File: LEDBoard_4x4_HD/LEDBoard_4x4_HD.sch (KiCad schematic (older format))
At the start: 24 parts, among them J1 power, J2 data, U1 TLC5957

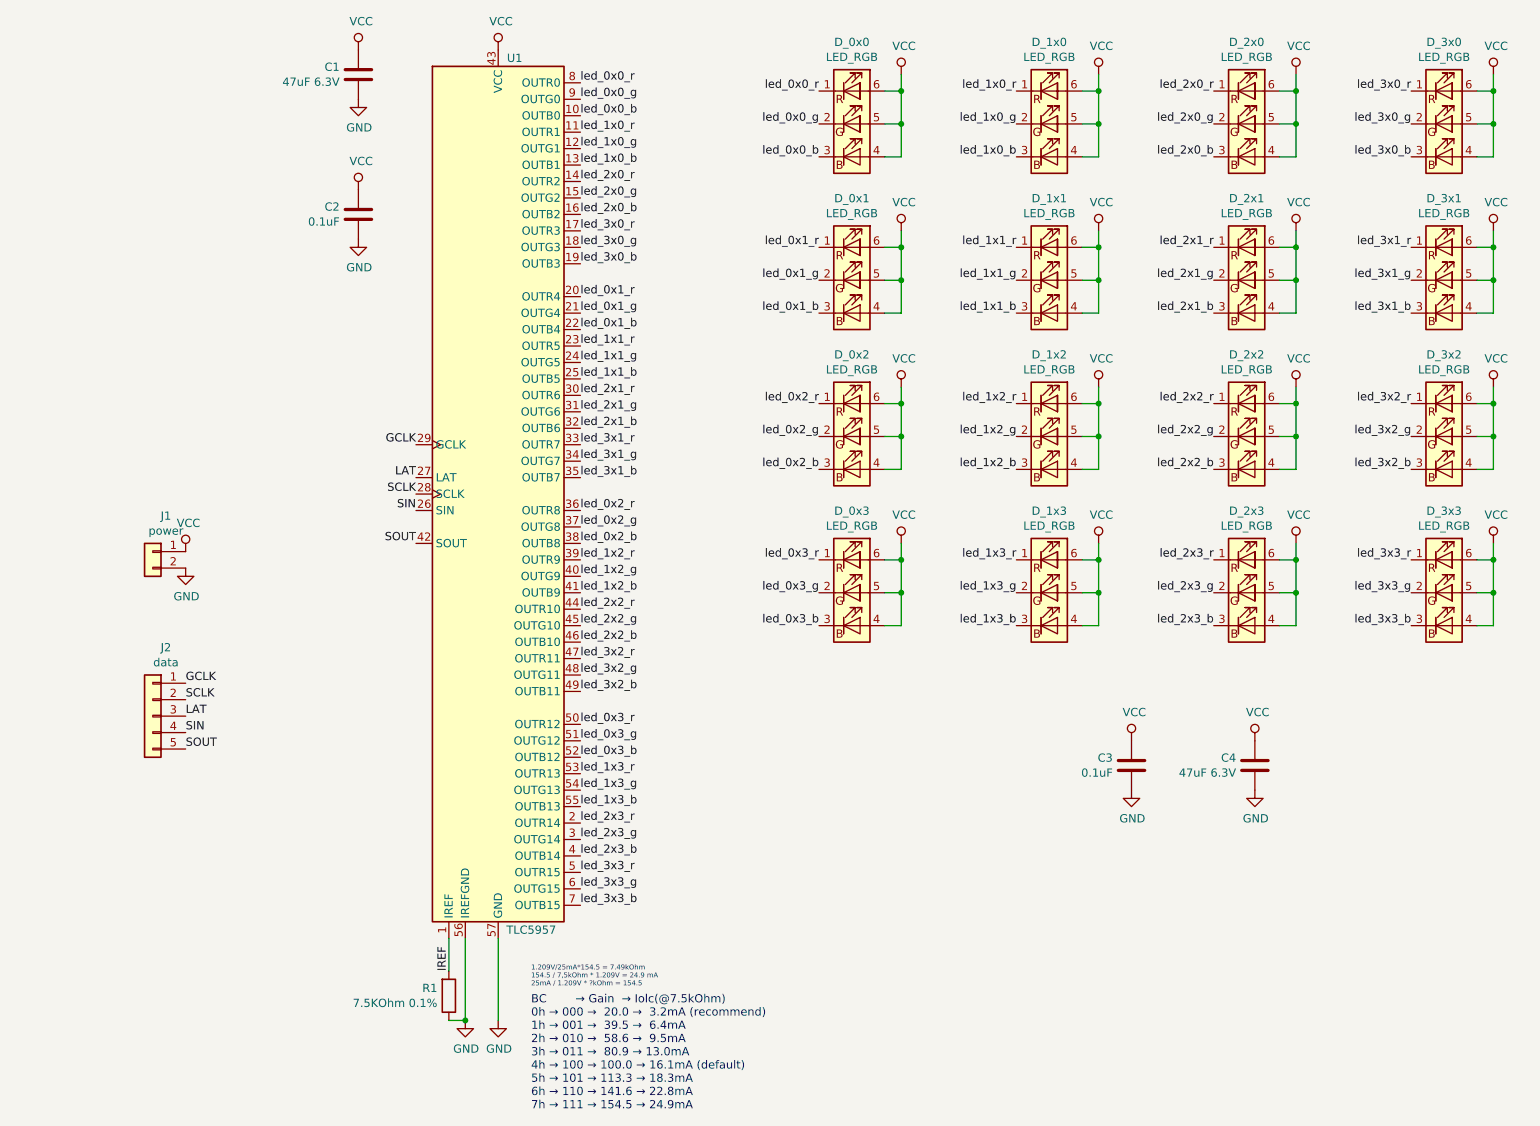
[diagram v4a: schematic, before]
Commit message: more layout tweeks + separate VCC for controler
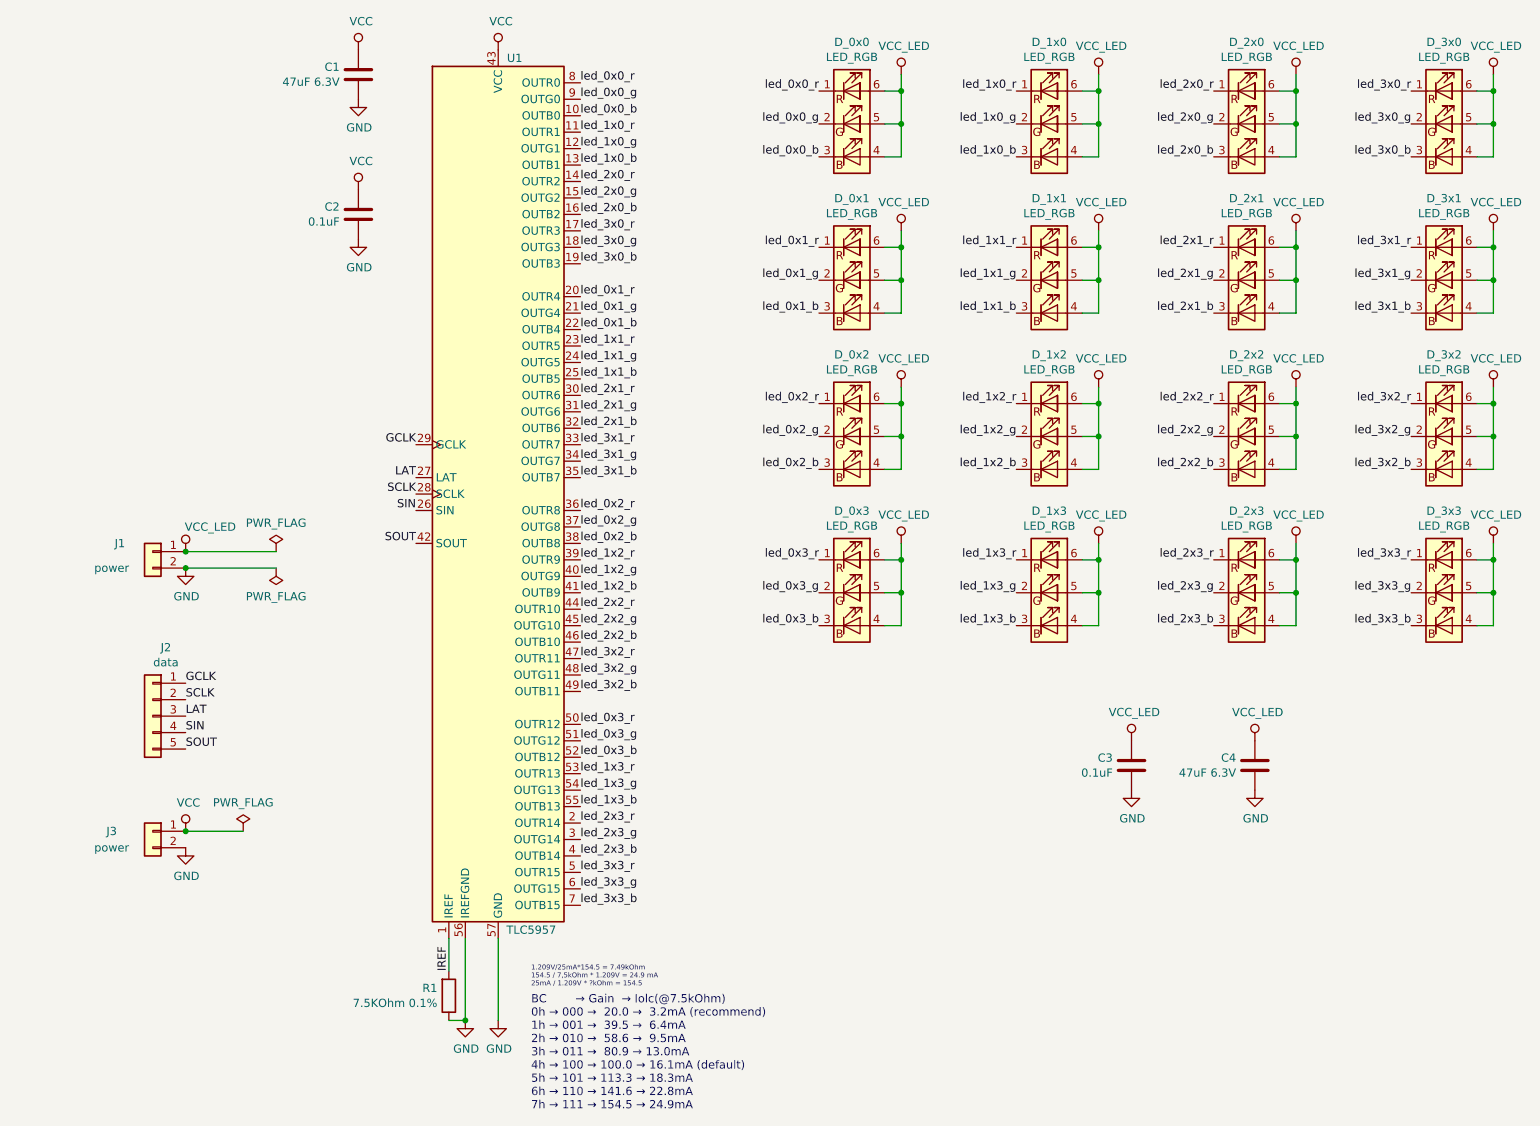
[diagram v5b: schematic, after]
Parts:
- added J3: power, PCB_SolderMount:Conn_01x02_SMD_90deg_SolderMount, symbol Connector_Generic:Conn_01x02
- J1: footprint Connector_PinHeader_2.54mm:PinHeader_1x02_P2.54mm_Vertical -> PCB_SolderMount:Conn_01x02_SMD_90deg_SolderMount
- J2: footprint Connector_PinHeader_2.54mm:PinHeader_1x05_P2.54mm_Vertical -> PCB_SolderMount:Conn_01x05_SMD_90deg_SolderMount
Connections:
- net GND: now also J3.2 (Pin_2)
- net VCC: now also J3.1 (Pin_1); no longer C3.2, C4.2, D_0x0.4 (BA), D_0x0.5 (GA), D_0x0.6 (RA), D_0x1.4 (BA), D_0x1.5 (GA), D_0x1.6 (RA), D_0x2.4 (BA), D_0x2.5 (GA), D_0x2.6 (RA), D_0x3.4 (BA), D_0x3.5 (GA), D_0x3.6 (RA), D_1x0.4 (BA), D_1x0.5 (GA), D_1x0.6 (RA), D_1x1.4 (BA), D_1x1.5 (GA), D_1x1.6 (RA), D_1x2.4 (BA), D_1x2.5 (GA), D_1x2.6 (RA), D_1x3.4 (BA), D_1x3.5 (GA), D_1x3.6 (RA), D_2x0.4 (BA), D_2x0.5 (GA), D_2x0.6 (RA), D_2x1.4 (BA), D_2x1.5 (GA), D_2x1.6 (RA), D_2x2.4 (BA), D_2x2.5 (GA), D_2x2.6 (RA), D_2x3.4 (BA), D_2x3.5 (GA), D_2x3.6 (RA), D_3x0.4 (BA), D_3x0.5 (GA), D_3x0.6 (RA), D_3x1.4 (BA), D_3x1.5 (GA), D_3x1.6 (RA), D_3x2.4 (BA), D_3x2.5 (GA), D_3x2.6 (RA), D_3x3.4 (BA), D_3x3.5 (GA), D_3x3.6 (RA), J1.1 (Pin_1)
- new net VCC_LED: C3.2, C4.2, D_0x0.4 (BA), D_0x0.5 (GA), D_0x0.6 (RA), D_0x1.4 (BA), D_0x1.5 (GA), D_0x1.6 (RA), D_0x2.4 (BA), D_0x2.5 (GA), D_0x2.6 (RA), D_0x3.4 (BA), D_0x3.5 (GA), D_0x3.6 (RA), D_1x0.4 (BA), D_1x0.5 (GA), D_1x0.6 (RA), D_1x1.4 (BA), D_1x1.5 (GA), D_1x1.6 (RA), D_1x2.4 (BA), D_1x2.5 (GA), D_1x2.6 (RA), D_1x3.4 (BA), D_1x3.5 (GA), D_1x3.6 (RA), D_2x0.4 (BA), D_2x0.5 (GA), D_2x0.6 (RA), D_2x1.4 (BA), D_2x1.5 (GA), D_2x1.6 (RA), D_2x2.4 (BA), D_2x2.5 (GA), D_2x2.6 (RA), D_2x3.4 (BA), D_2x3.5 (GA), D_2x3.6 (RA), D_3x0.4 (BA), D_3x0.5 (GA), D_3x0.6 (RA), D_3x1.4 (BA), D_3x1.5 (GA), D_3x1.6 (RA), D_3x2.4 (BA), D_3x2.5 (GA), D_3x2.6 (RA), D_3x3.4 (BA), D_3x3.5 (GA), D_3x3.6 (RA), J1.1 (Pin_1)
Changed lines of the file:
@@
 $EndComp
 $Comp
-L power:VCC #PWR0101
+L VCC_LED:VCC_LED #PWR0101
 U 1 1 5BC4D9F4
 P 7250 1900
 F 0 "#PWR0101" H 7250 1750 50  0001 C CNN
-F 1 "VCC" H 7267 2073 50  0000 C CNN
+F 1 "VCC_LED" H 7267 2073 50  0000 C CNN
 F 2 "" H 7250 1900 50  0001 C CNN
 F 3 "" H 7250 1900 50  0001 C CNN
@@
 $EndComp
 $Comp
-L power:VCC #PWR0102
+L VCC_LED:VCC_LED #PWR0102
 U 1 1 5BC4DBAD
 P 7250 950
 F 0 "#PWR0102" H 7250 800 50  0001 C CNN
-F 1 "VCC" H 7267 1123 50  0000 C CNN
+F 1 "VCC_LED" H 7267 1123 50  0000 C CNN
 F 2 "" H 7250 950 50  0001 C CNN
 F 3 "" H 7250 950 50  0001 C CNN
@@
 $EndComp
 $Comp
-L power:VCC #PWR0103
+L VCC_LED:VCC_LED #PWR0103
 U 1 1 5BC4DCEA
 P 7250 3800
 F 0 "#PWR0103" H 7250 3650 50  0001 C CNN
-F 1 "VCC" H 7267 3973 50  0000 C CNN
+F 1 "VCC_LED" H 7267 3973 50  0000 C CNN
 F 2 "" H 7250 3800 50  0001 C CNN
 F 3 "" H 7250 3800 50  0001 C CNN
@@
 $EndComp
 $Comp
-L power:VCC #PWR0104
+L VCC_LED:VCC_LED #PWR0104
 U 1 1 5BC4DD01
 P 7250 2850
 F 0 "#PWR0104" H 7250 2700 50  0001 C CNN
-F 1 "VCC" H 7267 3023 50  0000 C CNN
+F 1 "VCC_LED" H 7267 3023 50  0000 C CNN
 F 2 "" H 7250 2850 50  0001 C CNN
 F 3 "" H 7250 2850 50  0001 C CNN
@@
 $EndComp
 $Comp
-L power:VCC #PWR0105
+L VCC_LED:VCC_LED #PWR0105
 U 1 1 5BC4E1D5
 P 8450 1900
 F 0 "#PWR0105" H 8450 1750 50  0001 C CNN
-F 1 "VCC" H 8467 2073 50  0000 C CNN
+F 1 "VCC_LED" H 8467 2073 50  0000 C CNN
 F 2 "" H 8450 1900 50  0001 C CNN
 F 3 "" H 8450 1900 50  0001 C CNN
@@
 $EndComp
 $Comp
-L power:VCC #PWR0106
+L VCC_LED:VCC_LED #PWR0106
 U 1 1 5BC4E1EC
 P 8450 950
 F 0 "#PWR0106" H 8450 800 50  0001 C CNN
-F 1 "VCC" H 8467 1123 50  0000 C CNN
+F 1 "VCC_LED" H 8467 1123 50  0000 C CNN
 F 2 "" H 8450 950 50  0001 C CNN
 F 3 "" H 8450 950 50  0001 C CNN
@@
 $EndComp
 $Comp
-L power:VCC #PWR0107
+L VCC_LED:VCC_LED #PWR0107
 U 1 1 5BC4E203
 P 8450 3800
 F 0 "#PWR0107" H 8450 3650 50  0001 C CNN
-F 1 "VCC" H 8467 3973 50  0000 C CNN
+F 1 "VCC_LED" H 8467 3973 50  0000 C CNN
 F 2 "" H 8450 3800 50  0001 C CNN
 F 3 "" H 8450 3800 50  0001 C CNN
@@
 $EndComp
 $Comp
-L power:VCC #PWR0108
+L VCC_LED:VCC_LED #PWR0108
 U 1 1 5BC4E21A
 P 8450 2850
 F 0 "#PWR0108" H 8450 2700 50  0001 C CNN
-F 1 "VCC" H 8467 3023 50  0000 C CNN
+F 1 "VCC_LED" H 8467 3023 50  0000 C CNN
 F 2 "" H 8450 2850 50  0001 C CNN
 F 3 "" H 8450 2850 50  0001 C CNN
@@
 $EndComp
 $Comp
-L power:VCC #PWR0109
+L VCC_LED:VCC_LED #PWR0109
 U 1 1 5BC4EE04
 P 9650 1900
 F 0 "#PWR0109" H 9650 1750 50  0001 C CNN
-F 1 "VCC" H 9667 2073 50  0000 C CNN
+F 1 "VCC_LED" H 9667 2073 50  0000 C CNN
 F 2 "" H 9650 1900 50  0001 C CNN
 F 3 "" H 9650 1900 50  0001 C CNN
@@
 $EndComp
 $Comp
-L power:VCC #PWR0110
+L VCC_LED:VCC_LED #PWR0110
 U 1 1 5BC4EE1B
 P 9650 950
 F 0 "#PWR0110" H 9650 800 50  0001 C CNN
-F 1 "VCC" H 9667 1123 50  0000 C CNN
+F 1 "VCC_LED" H 9667 1123 50  0000 C CNN
 F 2 "" H 9650 950 50  0001 C CNN
 F 3 "" H 9650 950 50  0001 C CNN
@@
 $EndComp
 $Comp
-L power:VCC #PWR0111
+L VCC_LED:VCC_LED #PWR0111
 U 1 1 5BC4EE32
 P 9650 3800
 F 0 "#PWR0111" H 9650 3650 50  0001 C CNN
-F 1 "VCC" H 9667 3973 50  0000 C CNN
+F 1 "VCC_LED" H 9667 3973 50  0000 C CNN
 F 2 "" H 9650 3800 50  0001 C CNN
 F 3 "" H 9650 3800 50  0001 C CNN
@@
 $EndComp
 $Comp
-L power:VCC #PWR0112
+L VCC_LED:VCC_LED #PWR0112
 U 1 1 5BC4EE49
 P 9650 2850
 F 0 "#PWR0112" H 9650 2700 50  0001 C CNN
-F 1 "VCC" H 9667 3023 50  0000 C CNN
+F 1 "VCC_LED" H 9667 3023 50  0000 C CNN
 F 2 "" H 9650 2850 50  0001 C CNN
 F 3 "" H 9650 2850 50  0001 C CNN
@@
 $EndComp
 $Comp
-L power:VCC #PWR0113
+L VCC_LED:VCC_LED #PWR0113
 U 1 1 5BC4EE60
 P 10850 1900
 F 0 "#PWR0113" H 10850 1750 50  0001 C CNN
-F 1 "VCC" H 10867 2073 50  0000 C CNN
+F 1 "VCC_LED" H 10867 2073 50  0000 C CNN
 F 2 "" H 10850 1900 50  0001 C CNN
 F 3 "" H 10850 1900 50  0001 C CNN
@@
 $EndComp
 $Comp
-L power:VCC #PWR0114
+L VCC_LED:VCC_LED #PWR0114
 U 1 1 5BC4EE77
 P 10850 950
 F 0 "#PWR0114" H 10850 800 50  0001 C CNN
-F 1 "VCC" H 10867 1123 50  0000 C CNN
+F 1 "VCC_LED" H 10867 1123 50  0000 C CNN
 F 2 "" H 10850 950 50  0001 C CNN
 F 3 "" H 10850 950 50  0001 C CNN
@@
 $EndComp
 $Comp
-L power:VCC #PWR0115
+L VCC_LED:VCC_LED #PWR0115
 U 1 1 5BC4EE8E
 P 10850 3800
 F 0 "#PWR0115" H 10850 3650 50  0001 C CNN
-F 1 "VCC" H 10867 3973 50  0000 C CNN
+F 1 "VCC_LED" H 10867 3973 50  0000 C CNN
 F 2 "" H 10850 3800 50  0001 C CNN
 F 3 "" H 10850 3800 50  0001 C CNN
@@
 $EndComp
 $Comp
-L power:VCC #PWR0116
+L VCC_LED:VCC_LED #PWR0116
 U 1 1 5BC4EEA5
 P 10850 2850
 F 0 "#PWR0116" H 10850 2700 50  0001 C CNN
-F 1 "VCC" H 10867 3023 50  0000 C CNN
+F 1 "VCC_LED" H 10867 3023 50  0000 C CNN
 F 2 "" H 10850 2850 50  0001 C CNN
 F 3 "" H 10850 2850 50  0001 C CNN
@@
 U 1 1 5BCFD7B9
 P 2700 3850
-F 0 "J1" H 2620 4067 50  0000 C CNN
-F 1 "power" H 2620 3976 50  0000 C CNN
-F 2 "Connector_PinHeader_2.54mm:PinHeader_1x02_P2.54mm_Vertical" H 2700 3850 50  0001 C CNN
+F 0 "J1" H 2900 3900 50  0000 C CNN
+F 1 "power" H 2950 3750 50  0000 C CNN
+F 2 "PCB_SolderMount:Conn_01x02_SMD_90deg_SolderMount" H 2700 3850 50  0001 C CNN
 F 3 "~" H 2700 3850 50  0001 C CNN
 	1    2700 3850
@@
 $EndComp
 $Comp
-L power:VCC #PWR0120
+L VCC_LED:VCC_LED #PWR0120
 U 1 1 5BCFD851
 P 2900 3850
 F 0 "#PWR0120" H 2900 3700 50  0001 C CNN
-F 1 "VCC" H 2917 4023 50  0000 C CNN
+F 1 "VCC_LED" H 3050 4000 50  0000 C CNN
 F 2 "" H 2900 3850 50  0001 C CNN
 F 3 "" H 2900 3850 50  0001 C CNN
@@
 F 0 "J2" H 2620 5267 50  0000 C CNN
 F 1 "data" H 2620 5176 50  0000 C CNN
-F 2 "Connector_PinHeader_2.54mm:PinHeader_1x05_P2.54mm_Vertical" H 2700 4850 50  0001 C CNN
+F 2 "PCB_SolderMount:Conn_01x05_SMD_90deg_SolderMount" H 2700 4850 50  0001 C CNN
 F 3 "~" H 2700 4850 50  0001 C CNN
 	1    2700 4850
@@
 $EndComp
 $Comp
-L power:VCC #PWR0127
+L VCC_LED:VCC_LED #PWR0127
 U 1 1 5BD1A8E7
 P 8650 5000
 F 0 "#PWR0127" H 8650 4850 50  0001 C CNN
-F 1 "VCC" H 8667 5173 50  0000 C CNN
+F 1 "VCC_LED" H 8667 5173 50  0000 C CNN
 F 2 "" H 8650 5000 50  0001 C CNN
 F 3 "" H 8650 5000 50  0001 C CNN
@@
 $EndComp
 $Comp
-L power:VCC #PWR0129
+L VCC_LED:VCC_LED #PWR0129
 U 1 1 5BCD1F73
 P 9400 5000
 F 0 "#PWR0129" H 9400 4850 50  0001 C CNN
-F 1 "VCC" H 9417 5173 50  0000 C CNN
+F 1 "VCC_LED" H 9417 5173 50  0000 C CNN
 F 2 "" H 9400 5000 50  0001 C CNN
 F 3 "" H 9400 5000 50  0001 C CNN
@@
 	1    0    0    -1
 $EndComp
+$Comp
+L power:PWR_FLAG #FLG0101
+U 1 1 5BCE51BE
+P 3450 3950
+F 0 "#FLG0101" H 3450 4025 50  0001 C CNN
+F 1 "PWR_FLAG" H 3450 4123 50  0000 C CNN
+F 2 "" H 3450 3950 50  0001 C CNN
+F 3 "~" H 3450 3950 50  0001 C CNN
+	1    3450 3950
+	-1   0    0    1
+$EndComp
+Wire Wire Line
+	2900 3950 3450 3950
+$Comp
+L power:PWR_FLAG #FLG0102
+U 1 1 5BCE741F
+P 3450 3850
+F 0 "#FLG0102" H 3450 3925 50  0001 C CNN
+F 1 "PWR_FLAG" H 3450 4024 50  0000 C CNN
+F 2 "" H 3450 3850 50  0001 C CNN
+F 3 "~" H 3450 3850 50  0001 C CNN
+	1    3450 3850
+	1    0    0    -1
+$EndComp
+Wire Wire Line
+	3450 3850 2900 3850
+Connection ~ 2900 3850
+Connection ~ 2900 3950
+$Comp
+L Connector_Generic:Conn_01x02 J3
+U 1 1 5BCF9D83
+P 2700 5550
+F 0 "J3" H 2950 5550 50  0000 C CNN
+F 1 "power" H 2950 5450 50  0000 C CNN
+F 2 "PCB_SolderMount:Conn_01x02_SMD_90deg_SolderMount" H 2700 5550 50  0001 C CNN
+F 3 "~" H 2700 5550 50  0001 C CNN
+	1    2700 5550
+	-1   0    0    -1
+$EndComp
+$Comp
+L power:VCC #PWR0130
+U 1 1 5BCF9D89
+P 2900 5550
+F 0 "#PWR0130" H 2900 5400 50  0001 C CNN
+F 1 "VCC" H 2917 5723 50  0000 C CNN
+F 2 "" H 2900 5550 50  0001 C CNN
+F 3 "" H 2900 5550 50  0001 C CNN
+	1    2900 5550
+	1    0    0    -1
+$EndComp
+$Comp
+L power:GND #PWR0131
+U 1 1 5BCF9D8F
+P 2900 5650
+F 0 "#PWR0131" H 2900 5400 50  0001 C CNN
+F 1 "GND" H 2905 5477 50  0000 C CNN
+F 2 "" H 2900 5650 50  0001 C CNN
+F 3 "" H 2900 5650 50  0001 C CNN
+	1    2900 5650
+	1    0    0    -1
+$EndComp
+$Comp
+L power:PWR_FLAG #FLG?
+U 1 1 5BD0156F
+P 3250 5550
+F 0 "#FLG?" H 3250 5625 50  0001 C CNN
+F 1 "PWR_FLAG" H 3250 5724 50  0000 C CNN
+F 2 "" H 3250 5550 50  0001 C CNN
+F 3 "~" H 3250 5550 50  0001 C CNN
+	1    3250 5550
+	1    0    0    -1
+$EndComp
+Wire Wire Line
+	3250 5550 2900 5550
+Connection ~ 2900 5550
 $EndSCHEMATC
